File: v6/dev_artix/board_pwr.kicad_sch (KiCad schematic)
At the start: 72 parts, among them U101 LM3881MME_NOPB, U102 LTC3569EUDPBF, U103 LTC3569EUDPBF, U104 TPS51200DRCR

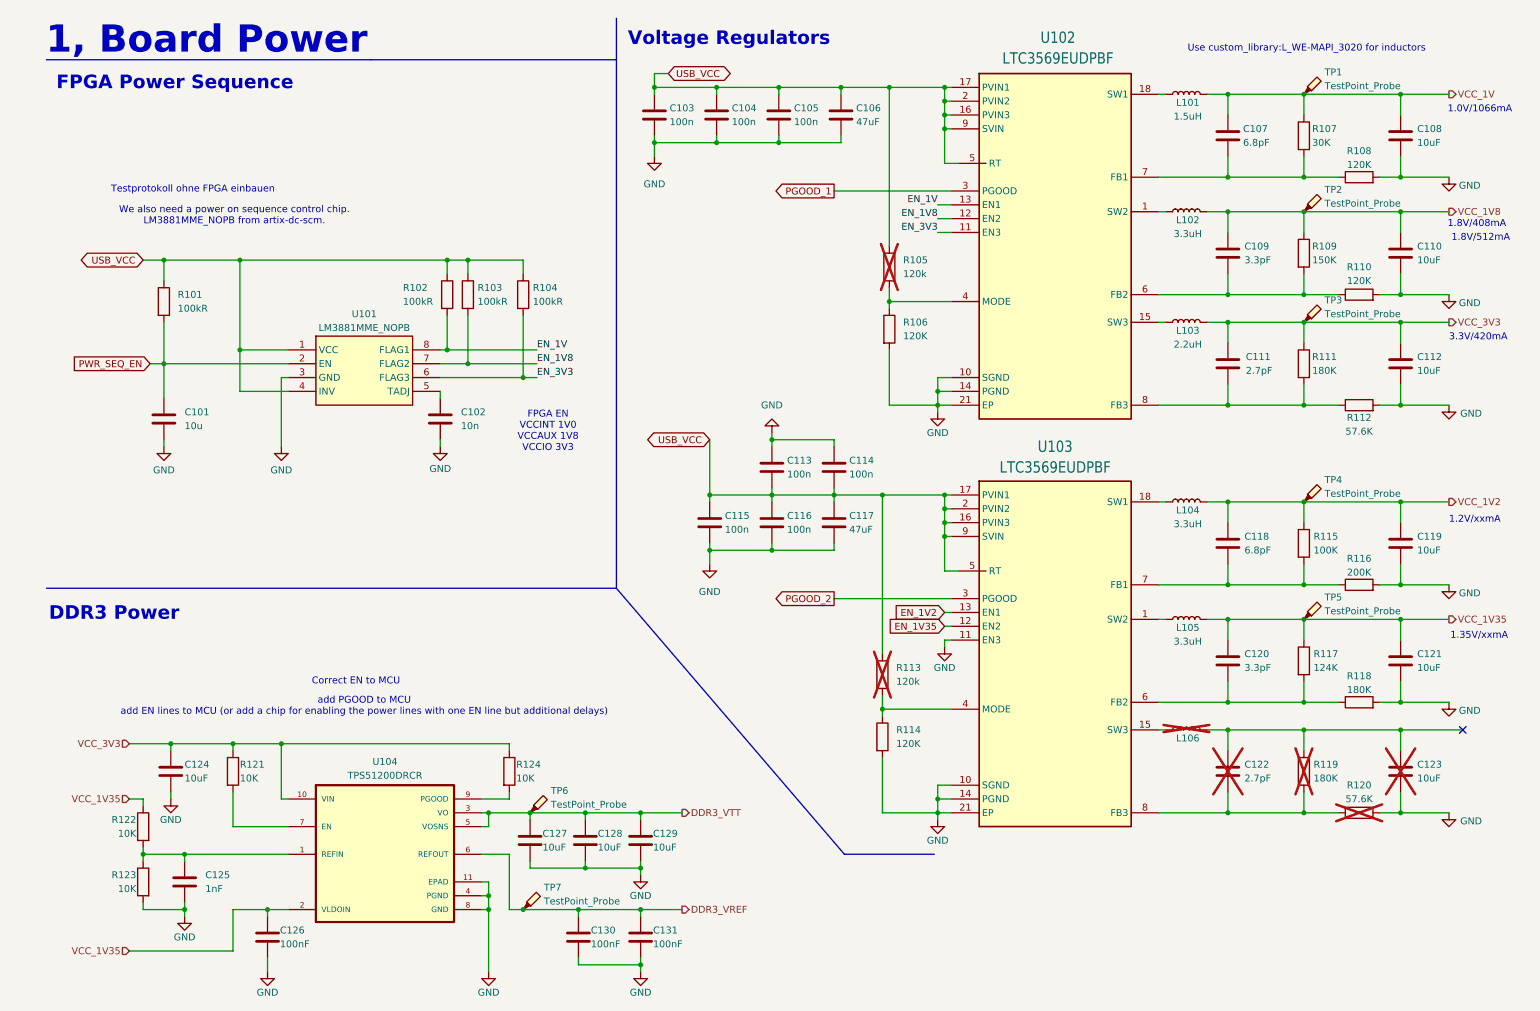
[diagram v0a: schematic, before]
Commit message: Adapt numbers for easier ordering and assembling
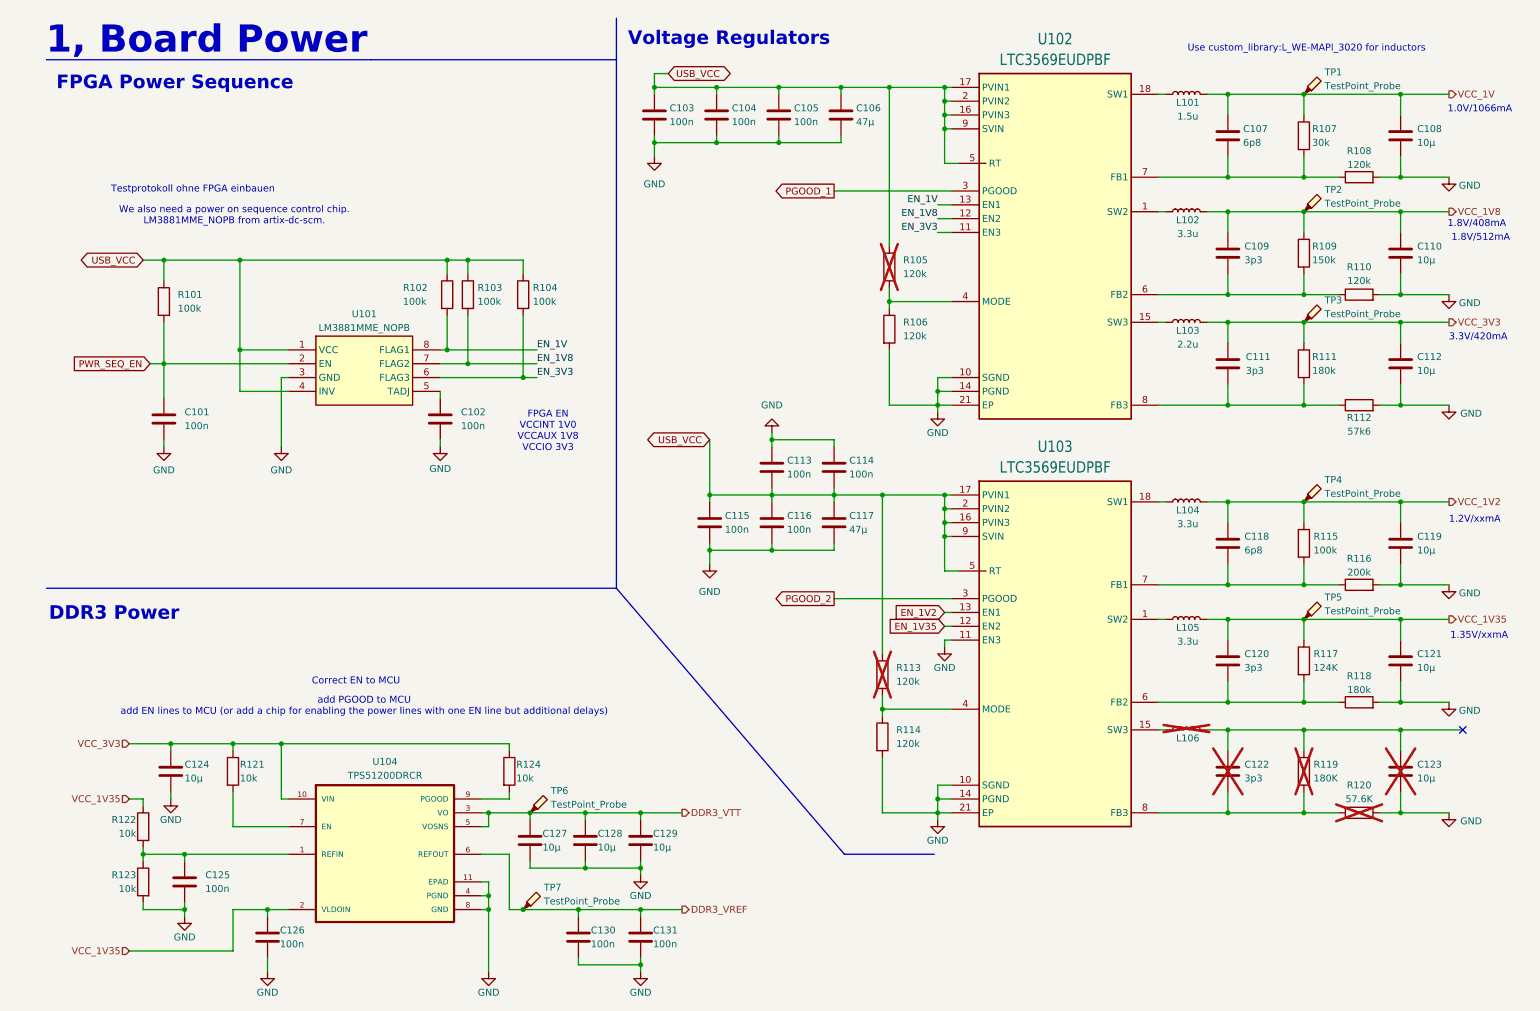
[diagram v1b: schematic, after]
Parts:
- C101: value 10u -> 100n
- C102: value 10n -> 100n
- C106, C117: value 47uF -> 47µ
- C107, C118: value 6.8pF -> 6p8
- C108, C110, C112, C119, C121, C123, C124, C127, C128, C129: value 10uF -> 10µ
- C109, C120: value 3.3pF -> 3p3
- C111, C122: value 2.7pF -> 3p3
- C125: value 1nF -> 100n
- C126, C130, C131: value 100nF -> 100n
- L101: value 1.5uH -> 1.5u
- L102, L104, L105: value 3.3uH -> 3.3u
- L103: value 2.2uH -> 2.2u
- R101, R102, R103, R104: value 100kR -> 100k
- R106, R108, R110, R114: value 120K -> 120k
- R107: value 30K -> 30k
- R109: value 150K -> 150k
- R111, R118: value 180K -> 180k
- R112: value 57.6K -> 57k6
- R115: value 100K -> 100k
- R116: value 200K -> 200k
- R121, R122, R123, R124: value 10K -> 10k
- TP1, TP2, TP3, TP4, TP5, TP6, TP7: now left out of the parts list
